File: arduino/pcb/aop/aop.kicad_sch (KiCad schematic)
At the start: 22 parts, among them Q1 AO4435, SW1 SW_Push, SW2 SW_Push, U1 ESP32-C3_SUPERMINI_TH, U2 DS3231M

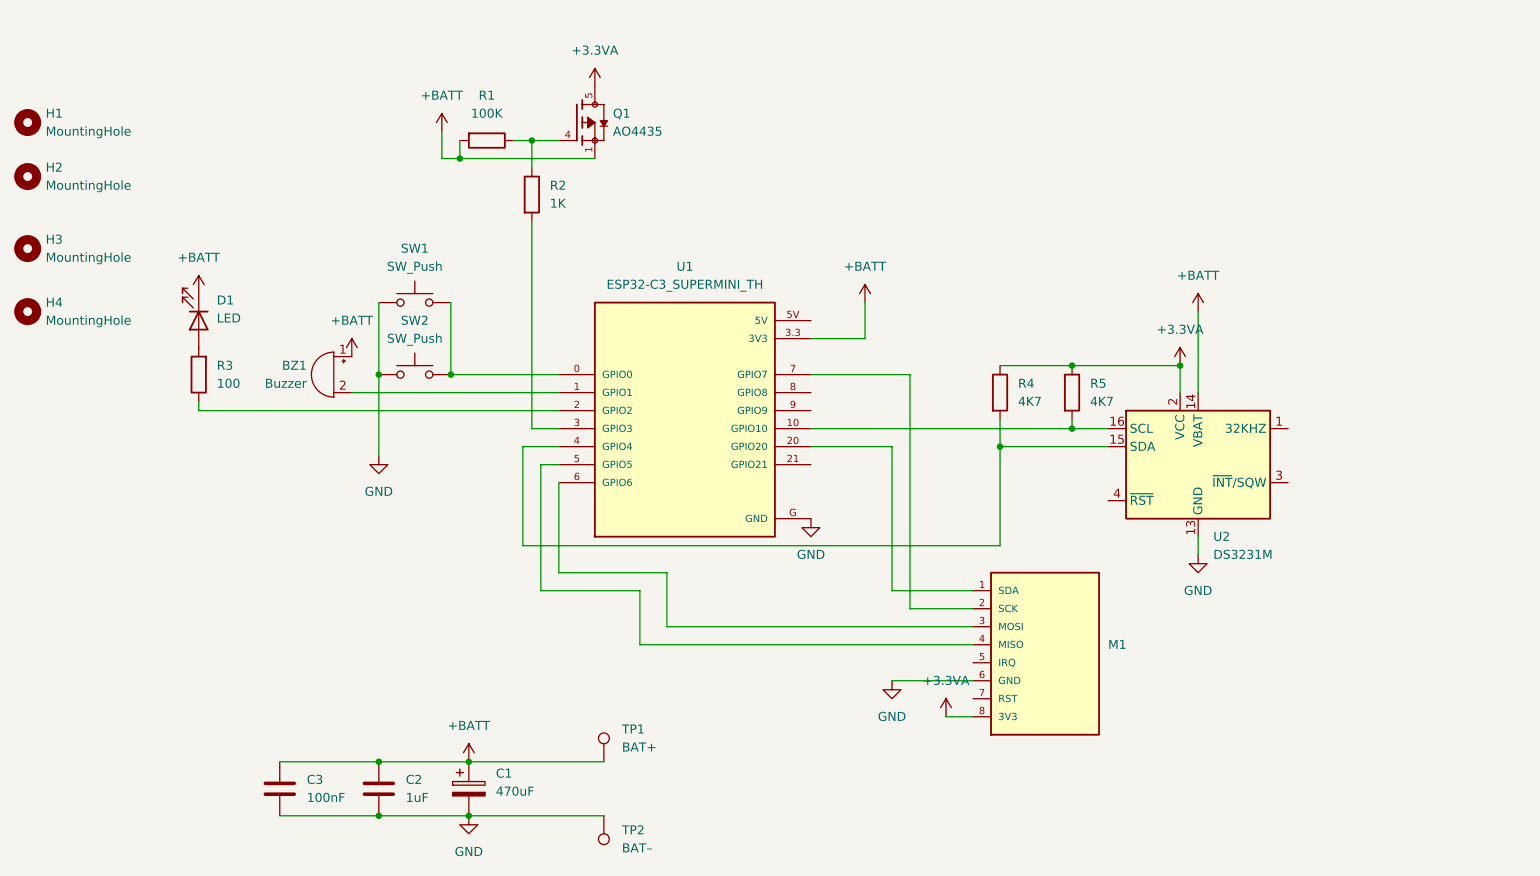
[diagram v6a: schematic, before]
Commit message: [pcb] Rearrange pins, combine buzzer and led to free UART
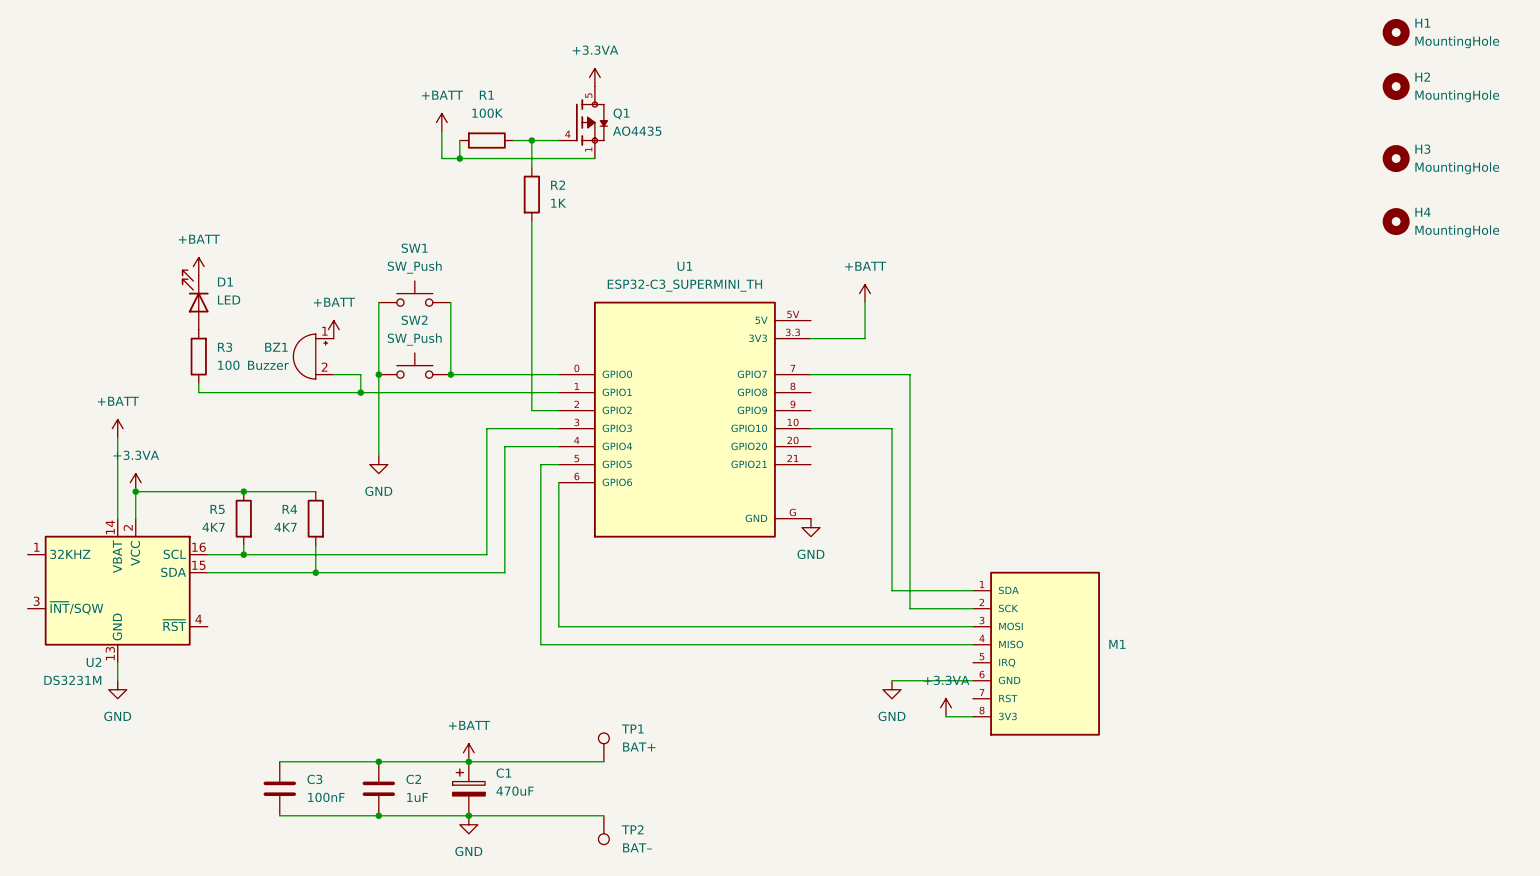
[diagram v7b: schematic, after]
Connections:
- net at R5.2, U2.16 (SCL): now also U1.3 (GPIO3); no longer U1.10 (GPIO10)
- net at R3.1: now also BZ1.2 (-), U1.1 (GPIO1); no longer U1.2 (GPIO2)
- net at M1.1 (SDA): now also U1.10 (GPIO10); no longer U1.20 (GPIO20)
- net at R2.2: now also U1.2 (GPIO2); no longer U1.3 (GPIO3)
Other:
- moved on the sheet: BZ1, D1, R3, R4, R5, U2

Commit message: [pcb] Expose UART0
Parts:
- added J1: UART, Connector_PinHeader_2.54mm:PinHeader_1x03_P2.54mm_Vertical, symbol Connector:Conn_01x03_Pin
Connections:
- net GND: now also J1.1 (Pin_1)
- net at U1.20 (GPIO20): now also J1.3 (Pin_3)
- net at U1.21 (GPIO21): now also J1.2 (Pin_2)
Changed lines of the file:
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@@
+	(wire
+		(pts
+			(xy 157.48 96.52) (xy 180.34 96.52)
+		)
+		(stroke
+			(width 0)
+			(type default)
+		)
+	)
 	(wire
 		(pts
@@
 		(pts
 			(xy 121.92 119.38) (xy 180.34 119.38)
+		)
+		(stroke
+			(width 0)
+			(type default)
+		)
+	)
+	(wire
+		(pts
+			(xy 157.48 93.98) (xy 180.34 93.98)
 		)
 		(stroke
@@
 	)
 	(symbol
+		(lib_id "power:GND")
+		(at 180.34 99.06 0)
+		(unit 1)
+		(body_style 1)
+		(exclude_from_sim no)
+		(in_bom yes)
+		(on_board yes)
+		(in_pos_files yes)
+		(dnp no)
+		(fields_autoplaced yes)
+		(property "Reference" "#PWR012"
+			(at 180.34 105.41 0)
+			(hide yes)
+			(show_name no)
+			(do_not_autoplace no)
+			(effects
+				(font
+					(size 1.27 1.27)
+				)
+			)
+		)
+		(property "Value" "GND"
+			(at 180.34 104.14 0)
+			(show_name no)
+			(do_not_autoplace no)
+			(effects
+				(font
+					(size 1.27 1.27)
+				)
+			)
+		)
+		(property "Footprint" ""
+			(at 180.34 99.06 0)
+			(hide yes)
+			(show_name no)
+			(do_not_autoplace no)
+			(effects
+				(font
+					(size 1.27 1.27)
+				)
+			)
+		)
+		(property "Datasheet" ""
+			(at 180.34 99.06 0)
+			(hide yes)
+			(show_name no)
+			(do_not_autoplace no)
+			(effects
+				(font
+					(size 1.27 1.27)
+				)
+			)
+		)
+		(property "Description" "Power symbol creates a global label with name \"GND\" , ground"
+			(at 180.34 99.06 0)
+			(hide yes)
+			(show_name no)
+			(do_not_autoplace no)
+			(effects
+				(font
+					(size 1.27 1.27)
+				)
+			)
+		)
+		(pin "1"
+		)
+		(instances
+			(project "aop"
+				(path "/6c2f9cd3-2815-4cb2-b88c-9d452fcffe7c"
+					(reference "#PWR012")
+					(unit 1)
+				)
+			)
+		)
+	)
+	(symbol
 		(lib_id "power:+BATT")
 		(at 59.69 92.71 0)
@@
 					(unit 1)
 				)
+			)
+		)
+	)
+	(symbol
+		(lib_id "Connector:Conn_01x03_Pin")
+		(at 185.42 96.52 180)
+		(unit 1)
+		(body_style 1)
+		(exclude_from_sim no)
+		(in_bom yes)
+		(on_board yes)
+		(in_pos_files yes)
+		(dnp no)
+		(property "Reference" "J1"
+			(at 184.785 104.14 0)
+			(show_name no)
+			(do_not_autoplace no)
+			(effects
+				(font
+					(size 1.27 1.27)
+				)
+			)
+		)
+		(property "Value" "UART"
+			(at 184.785 101.6 0)
+			(show_name no)
+			(do_not_autoplace no)
+			(effects
+				(font
+					(size 1.27 1.27)
+				)
+			)
+		)
+		(property "Footprint" "Connector_PinHeader_2.54mm:PinHeader_1x03_P2.54mm_Vertical"
+			(at 185.42 96.52 0)
+			(hide yes)
+			(show_name no)
+			(do_not_autoplace no)
+			(effects
+				(font
+					(size 1.27 1.27)
+				)
+			)
+		)
+		(property "Datasheet" ""
+			(at 185.42 96.52 0)
+			(hide yes)
+			(show_name no)
+			(do_not_autoplace no)
+			(effects
+				(font
+					(size 1.27 1.27)
+				)
+			)
+		)
+		(property "Description" "Generic connector, single row, 01x03, script generated"
+			(at 185.42 96.52 0)
+			(hide yes)
+			(show_name no)
+			(do_not_autoplace no)
+			(effects
+				(font
+					(size 1.27 1.27)
+				)
+			)
+		)
+		(pin "1"
+		)
+		(pin "2"
+		)
+		(pin "3"
+		)
+		(instances
+			(project "aop"
+				(path "/6c2f9cd3-2815-4cb2-b88c-9d452fcffe7c"
+					(reference "J1")
+					(unit 1)
+				)
